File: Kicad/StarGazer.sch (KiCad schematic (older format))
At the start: 18 parts

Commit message: Continued devolopment -Added battery charging circuit -Added power toggle to prevent over charging battery -Added voltage regulator
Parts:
- added C2, C?: 1uF, symbol Device:C
- added C? (x2): 4.7uF, symbol Device:C
- added D1, D2: LED, symbol Device:LED
- added J1: Conn_02x01 BATTERY, symbol Connector_Generic:Conn_02x01
- added R3: 10k, symbol Device:R
- added R5, R6: R_LED_BRIGHT, symbol Device:R_Small
- added R? (x2): R_PULLUP, symbol Device:R
- added SW?: SW_DIP_x01, symbol Switch:SW_DIP_x01
- added U2: STBC08, symbol StarGazer:STBC08
- added U?: AP22811BW5, Package_TO_SOT_SMD:TSOT-23-5_HandSoldering, symbol StarGazer:AP22811BW5
- added U?: AP2114H-1.8, Package_TO_SOT_SMD:SOT-223-3_TabPin2, symbol StarGazer:AP2114H-1.8
- SW1: renamed from SW?; value SW_Push -> RESET PUSH
- gave numbers to parts that had none: 17
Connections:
- net labels added: V_BATT, V_BATT_T, V_REG, V_USB
- net labels removed: 3V3
- wire segments 91 -> 143
- no-connect marks 0 -> 1
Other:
- note added: "10k PROG allows for 100mA from BATT."
- note added: "BATTERY CHARGING\n"
- note added: "POWER TOGGLE"
- note added: "VOLT REGULATOR\n"
- moved on the sheet: C1, R1, SW1

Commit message: Added screen, gyro, and magnometer. Updated schematic parts.
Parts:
- added C?: 100nF, symbol Device:C
- added C?: 2.2uF, symbol Device:C
- added J?: I2C_CONNECTOR_OUT, symbol Connector:Conn_01x04_Male
- added R? (x2): R_I2C_PULLUP, symbol Device:R
- added U?: LSM6DS33TR, Package_LGA:LGA-16_3x3mm_P0.5mm_LayoutBorder3x5y, symbol StarGazer:LSM6DS33TR
- added U?: MMC5603NJ, symbol StarGazer:MMC5603NJ
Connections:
- net V_BATT_T is gone; now on net V_BATT: C?.2, SW?.2, U?.3 (VIN)
- net GND: now also C?.1, C?.2, J?.1 (Pin_1), U?.10 (RES), U?.11 (RES), U?.12 (GND), U?.13 (GND), U?.15 (RES), U?.4 (SA0), U?.4 (VDD), U?.6 (INT2), U?.7 (INT1), U?.8 (RES), U?.9 (RES)
- net I2C_SCL: now also J?.2 (Pin_2), R?.2, U?.2 (SCL), U?.2 (SCL)
- net I2C_SDA: now also J?.3 (Pin_3), R?.2, U?.3 (SDA), U?.3 (SDA)
- net V_REG: now also C?.1, C?.2, J?.4 (Pin_4), R?.1, R?.1, U?.1 (VDDIO), U?.1 (VSA), U?.16 (VDD), U?.5 (CS)
- no-connect marks 1 -> 2
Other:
- note added: "GYRO"
- note added: "I2C"
- note added: "MAGNOMETER"
- moved on the sheet: C1, C5, C6, C7, C?, D4, R1, R8, SW1, U3, U4, U5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

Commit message: Changed linear voltage regulator from 1.7v to 2.8v This is done as I will be removing voltage regulators from some external parts (GPS, screen) and wiring in V_REG directly to them.  These usually take 3.3v, which I can't give them.
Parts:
- removed C?: 4.7uF, symbol Device:C
- removed U?: AP2114H-1.8, Package_TO_SOT_SMD:SOT-223-3_TabPin2, symbol StarGazer:AP2114H-1.8
- added C?: 1.0uF, symbol Device:C
- added D? (x23): RING_LED, symbol Device:LED
- added J? (x2): I2C_CONNECTOR_OUT, symbol Connector:Conn_01x04_Male
- added R? (x23): R_LED_RING, symbol Device:R
- added U?: TLV75528PDBV, Package_TO_SOT_SMD:SOT-23-5, symbol Regulator_Linear:TLV75528PDBV
- C?: value 4.7uF -> 1.0uF
- D4: value LED -> RING_LED
- R8: value R -> R_LED_RING
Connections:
- net GND: now also C?.1, D?.1 (K), D?.1 (K), D?.1 (K), D?.1 (K), D?.1 (K), D?.1 (K), D?.1 (K), D?.1 (K), D?.1 (K), D?.1 (K), D?.1 (K), D?.1 (K), D?.1 (K), D?.1 (K), D?.1 (K), D?.1 (K), D?.1 (K), D?.1 (K), D?.1 (K), D?.1 (K), D?.1 (K), D?.1 (K), D?.1 (K), J?.1 (Pin_1), J?.1 (Pin_1), U?.2 (GND), U?.4 (NC)
- net I2C_SCL: now also J?.2 (Pin_2), J?.2 (Pin_2)
- net I2C_SDA: now also J?.3 (Pin_3), J?.3 (Pin_3)
- net V_BATT: now also U?.1 (IN), U?.3 (EN)
- net V_REG: now also C?.2, J?.4 (Pin_4), J?.4 (Pin_4), U?.5 (OUT)
- net ADC_IN1: now reaches U1.7 (PA1)
- net at U3.1 (Q1): now also R?.2
- net at U3.2 (Q2): now also R?.2
- net at U3.3 (Q3): now also R?.2
- net at U3.4 (Q4): now also R?.2
- net at U3.5 (Q5): now also R?.2
- net at U3.6 (Q6): now also R?.2
- net at U3.7 (Q7): now also R?.2
- net at U4.1 (Q1): now also R?.2
- net at U4.15 (Q0): now also R?.2
- net at U4.2 (Q2): now also R?.2
- net at U4.3 (Q3): now also R?.2
- net at U4.4 (Q4): now also R?.2
- net at U4.5 (Q5): now also R?.2
- net at U4.6 (Q6): now also R?.2
- net at U4.7 (Q7): now also R?.2
- net at U5.1 (Q1): now also R?.2
- net at U5.15 (Q0): now also R?.2
- net at U5.2 (Q2): now also R?.2
- net at U5.3 (Q3): now also R?.2
- net at U5.4 (Q4): now also R?.2
- net at U5.5 (Q5): now also R?.2
- net at U5.6 (Q6): now also R?.2
- net at U5.7 (Q7): now also R?.2
- new net: D?.2 (A), R?.1 (x23)
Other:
- note added: "GPS\n"
- note added: "SCREEN\n"
- note added: "SHIFT REGISTERS"
- note added: "V_REG = 2.8V\n"
- moved on the sheet: C1, C2, C3, C4, C5, C6, C7, C?, D1, D2, D3, D4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

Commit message: Added oscillator.
Primary part selection is complete.
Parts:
- added C? (x2): 4pF, symbol Device:C_Small
- added J?: CONN_JOYSTICK, symbol Connector:Conn_01x05_Male
- added RV?: R_POT, symbol Device:R_POT
- added U?: TSX-3225, Kicad:TSX-3225, symbol StarGazer:TSX-3225
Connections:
- net GND: now also C?.2, C?.2, J?.1 (Pin_1), U?.4 (GND)
- net OSC_IN: now also C?.1, U?.1 (OSC_IN)
- net OSC_OUT: now also RV?.2
- net V_REG: now also J?.5 (Pin_5)
- net UI_BUTTON: now reaches U1.14 (PB1)
- net UI_BUTTON: now also J?.2 (Pin_2)
- net UI_JOY_Y: now reaches U1.8 (PA2)
- net UI_JOY_Y: now also J?.4 (Pin_4)
- net ADC_IN1 renamed UI_JOY_X
- net UI_JOY_X: now also J?.3 (Pin_3)
- new net: C?.1, RV?.3, U?.3 (OSC_OUT)
- no-connect marks 2 -> 3
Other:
- note added: "OSCILLATOR\n16MHZ"
- note added: "UI\n"
- moved on the sheet: C1, C2, C5, C6, C7, C?, D1, D2, D4, D?, J1, J?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

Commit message: Assigning foot prints and testing GitHub as a site to document project with images.
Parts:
- removed D3: LED, symbol Device:LED
- removed R4: R_LED, symbol Device:R
- C1: part_details (none) -> part details; part_name (none) -> part name example; part_url (none) -> some.part.url.com
- R1: value R_PULLUP -> 10k; footprint (none) -> Resistor_SMD:R_1206_3216Metric_Pad1.42x1.75mm_HandSolder; part_name (none) -> Resistor - Pull Up; part_url (none) -> https://www.digikey.com/product-detail/en/yageo/RC1206JR-07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
- R10, R9: renamed from R?; value R_PULLUP -> 10k; footprint (none) -> Resistor_SMD:R_1206_3216Metric_Pad1.42x1.75mm_HandSolder; part_name (none) -> Resistor - Pull Up; part_url (none) -> https://www.digikey.com/product-detail/en/yageo/RC1206JR-07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
- R2, R7: value R_High -> 10k; footprint (none) -> Resistor_SMD:R_1206_3216Metric_Pad1.42x1.75mm_HandSolder; part_name (none) -> Resistor - Pull Up; part_url (none) -> https://www.digikey.com/product-detail/en/yageo/RC1206JR-07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
- R3: footprint (none) -> Resistor_SMD:R_1206_3216Metric_Pad1.42x1.75mm_HandSolder; part_details (none) -> Battery Program for 100mA recharge rate.; part_name (none) -> Resistor - Prog; part_url (none) -> https://www.digikey.com/product-detail/en/yageo/RC1206JR-07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
- R5, R6: value R_LED_BRIGHT -> 200; footprint (none) -> Resistor_SMD:R_1206_3216Metric_Pad1.42x1.75mm_HandSolder; part_name (none) -> Resistor - LED Status; part_url (none) -> https://www.digikey.com/product-detail/en/yageo/RC1206FR-07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
- RV1: renamed from RV?; footprint (none) -> Kicad:35WR10KLFTR; part_details (none) -> Adjustable external clock resistor.; part_name (none) -> Resistor - Potentiometer; part_url (none) -> https://www.digikey.com/product-detail/en/tt-electronics-bi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
- U1: part_details (none) -> Cortex M0 48MHz; part_name (none) -> STM32F070F6P6TR; part_url (none) -> https://www.digikey.com/product-detail/en/stmicroelectronic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
- U10: renamed from U?; part_details (none) -> 6-axis Gyrometer; part_name (none) -> LSM6DS33TR; part_url (none) -> https://www.digikey.com/product-detail/en/stmicroelectronic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
- U2: part_details (none) -> Lithium Ion Battery Recharge IC; part_name (none) -> STBC08PMR; part_url (none) -> https://www.digikey.com/product-detail/en/stmicroelectronic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
- U3, U4, U5: part_details (none) -> Shift Register; part_name (none) -> 74HC595D,118; part_url (none) -> https://www.digikey.com/product-detail/en/nexperia-usa-inc/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
- U6: renamed from U?; part_details (none) -> Mosfet, active low (batt protection); part_name (none) -> AP22811BW5-7; part_url (none) -> https://www.digikey.com/product-detail/en/diodes-incorporat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
- U7: renamed from U?; part_details (none) -> Linear Regulator, 2.8v 500mA, 230mV~ dropout; part_name (none) -> TLV75528PDBVR; part_url (none) -> https://www.digikey.com/product-detail/en/texas-instruments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
- U8: renamed from U?; part_details (none) -> 16MHz Crystal; part_name (none) -> TSX-3225; part_url (none) -> https://www.digikey.com/product-detail/en/epson/TSX-3225-16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
- U9: renamed from U?; part_details (none) -> Magnometer Sensor; part_name (none) -> MMC5603NJ; part_url (none) -> https://www.digikey.com/product-detail/en/memsic-inc/MMC560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
- gave numbers to parts that had none: 60

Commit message: Moved major schematic parts to their own sheets - unknown if they have brought about issues because of this. Updated reference IDs.
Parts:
- removed C1: 0.1 uF, symbol Device:C
- removed C10, C9: 1.0uF, symbol Device:C
- removed C11, C12: 4pF, symbol Device:C_Small
- removed C13: 2.2uF, symbol Device:C
- removed C14: 100nF, symbol Device:C
- removed C2, C8: 1uF, symbol Device:C
- removed C5, C6, C7: 10uF, symbol Device:CP
- removed D1, D2: LED, symbol Device:LED
- removed D10, D11, D12, D13, D14, D15, D16, D17, D18, D19, D20, D21, D22, D23, D24, D25, D26, D27, D4, D5, D6, D7, D8, D9: RING_LED, symbol Device:LED
- removed J1: Conn_02x01 BATTERY, symbol Connector_Generic:Conn_02x01
- removed J2, J3, J5: I2C_CONNECTOR_OUT, symbol Connector:Conn_01x04_Male
- removed J4: CONN_JOYSTICK, symbol Connector:Conn_01x05_Male
- removed R1, R10, R3, R9: 10k, Resistor_SMD:R_1206_3216Metric_Pad1.42x1.75mm_HandSolder, symbol Device:R
- removed R11, R12, R13, R14, R15, R16, R17, R18, R19, R20, R21, R22, R23, R24, R25, R26, R27, R28, R29, R30, R31, R32, R33, R8: R_LED_RING, symbol Device:R
- removed R34, R35: R_I2C_PULLUP, symbol Device:R
- removed R5, R6: 200, Resistor_SMD:R_1206_3216Metric_Pad1.42x1.75mm_HandSolder, symbol Device:R_Small
- removed RV1: R_POT, Kicad:35WR10KLFTR, symbol Device:R_POT
- removed SW1: RESET PUSH, symbol Switch:SW_Push
- removed SW2: SW_DIP_x01, symbol Switch:SW_DIP_x01
- removed U10: LSM6DS33TR, Package_LGA:LGA-16_3x3mm_P0.5mm_LayoutBorder3x5y, symbol StarGazer:LSM6DS33TR
- removed U2: STBC08, symbol StarGazer:STBC08
- removed U3, U4, U5: 74HC595D, Kicad:StarGazer_74HC595D_SOIC-16, symbol StarGazer:74HC595D
- removed U6: AP22811BW5, Package_TO_SOT_SMD:TSOT-23-5_HandSoldering, symbol StarGazer:AP22811BW5
- removed U7: TLV75528PDBV, Package_TO_SOT_SMD:SOT-23-5, symbol Regulator_Linear:TLV75528PDBV
- removed U8: TSX-3225, Kicad:TSX-3225, symbol StarGazer:TSX-3225
- removed U9: MMC5603NJ, symbol StarGazer:MMC5603NJ
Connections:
- no-connect marks 3 -> 0
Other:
- note removed: "10k PROG allows for 100mA from BATT."
- note removed: "BATTERY CHARGING\n"
- note removed: "GPS\n"
- note removed: "GYRO"
- note removed: "I2C"
- note removed: "MAGNOMETER"
- note removed: "OSCILLATOR\n16MHZ"
- note removed: "POWER TOGGLE"
- note removed: "RESET DIAGRAM"
- note removed: "SCREEN\n"
- note removed: "SHIFT REGISTERS"
- note removed: "UI\n"
- note removed: "VOLT REGULATOR\n"
- note removed: "V_REG = 2.8V\n"

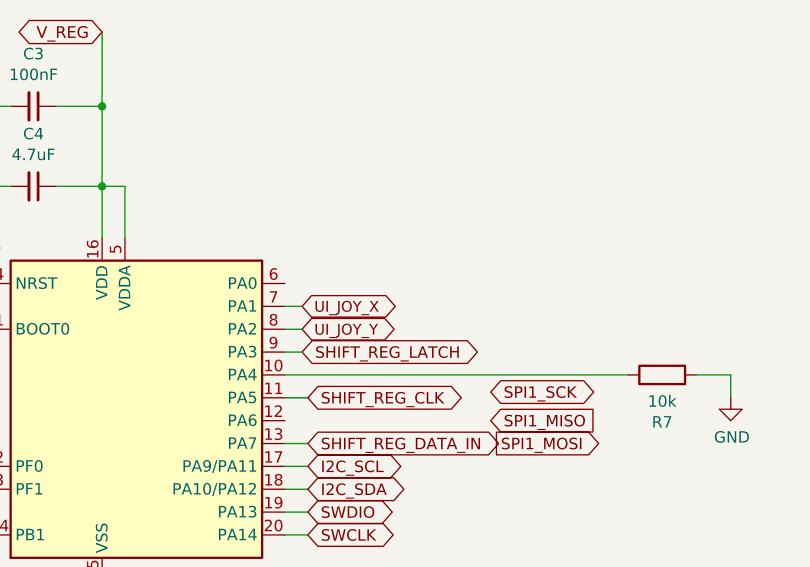
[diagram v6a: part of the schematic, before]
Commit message: Corrected some schematic labeling.
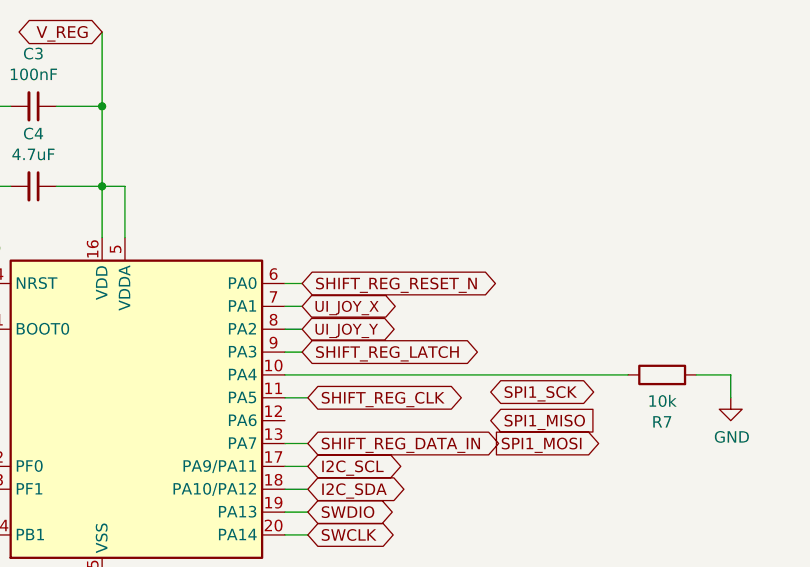
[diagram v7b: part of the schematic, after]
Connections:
- net SHIFT_REG_RESET_N: now reaches U1.6 (PA0)
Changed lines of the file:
@@
 F1 "Schematic_Test_Digital.sch" 50
 $EndSheet
+Text GLabel 6175 3275 2    50   BiDi ~ 0
+SHIFT_REG_RESET_N
+Wire Wire Line
+	6100 3275 6175 3275
 $EndSCHEMATC
